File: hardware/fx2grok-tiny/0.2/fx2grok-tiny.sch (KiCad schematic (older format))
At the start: 27 parts, among them IC1 CY7C68013A-56, P1 CONN_01X05, P2 CONN_01X05, U1 MICRO-USB-B-SMD, U2 MIC5504, Y1 24MHz

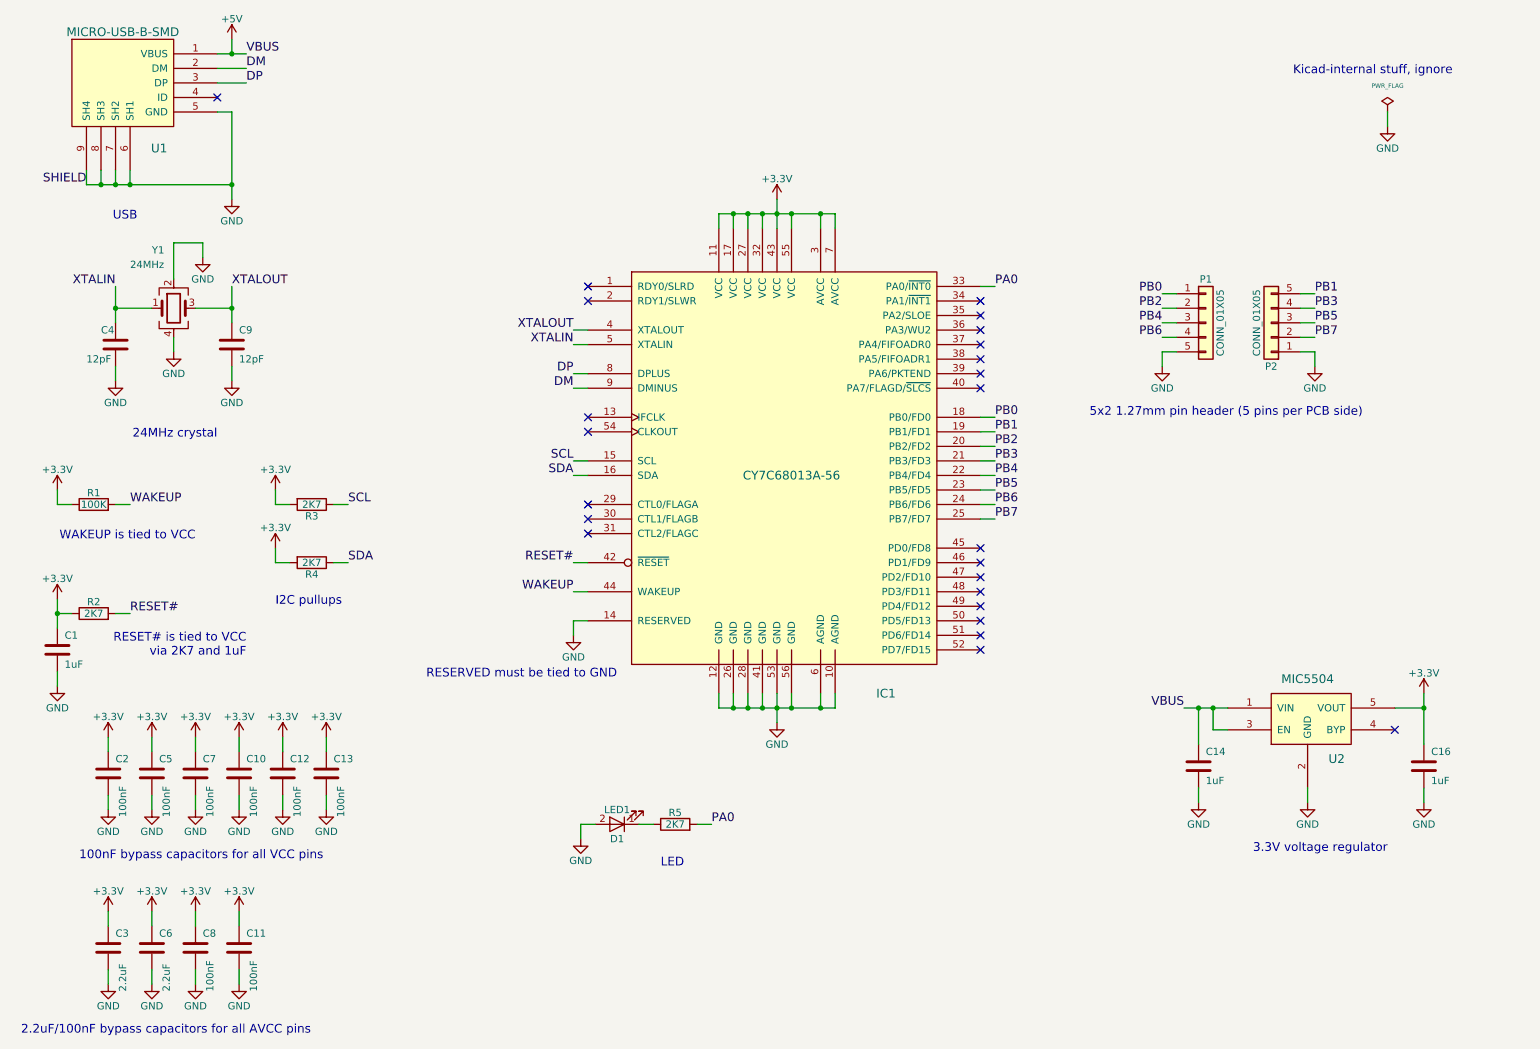
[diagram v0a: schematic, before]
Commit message: fx2grok-tiny: Reroute PCB from scratch with various changes.
 - The previously incorrect FX2 footprint is fixed now.

 - The FX2's thermal pad is set to GND now.

 - The FX2 footprint now has a dot on the copper as well as on the
   silkscreen for pin 1.

 - The PCB is now 11x11mm (instead of 13x13mm).

 - The 1.27mm pin header connectors are shortened and the pinout changed.

 - The trace clearance changed from 6mil to 5mil.

 - The USB connector footprint now has two oval pads (space reasons).

 - The LED is now connected to PA1 (not PA0).

 - The schematics/layout license is changed to CC-BY-SA 4.0.
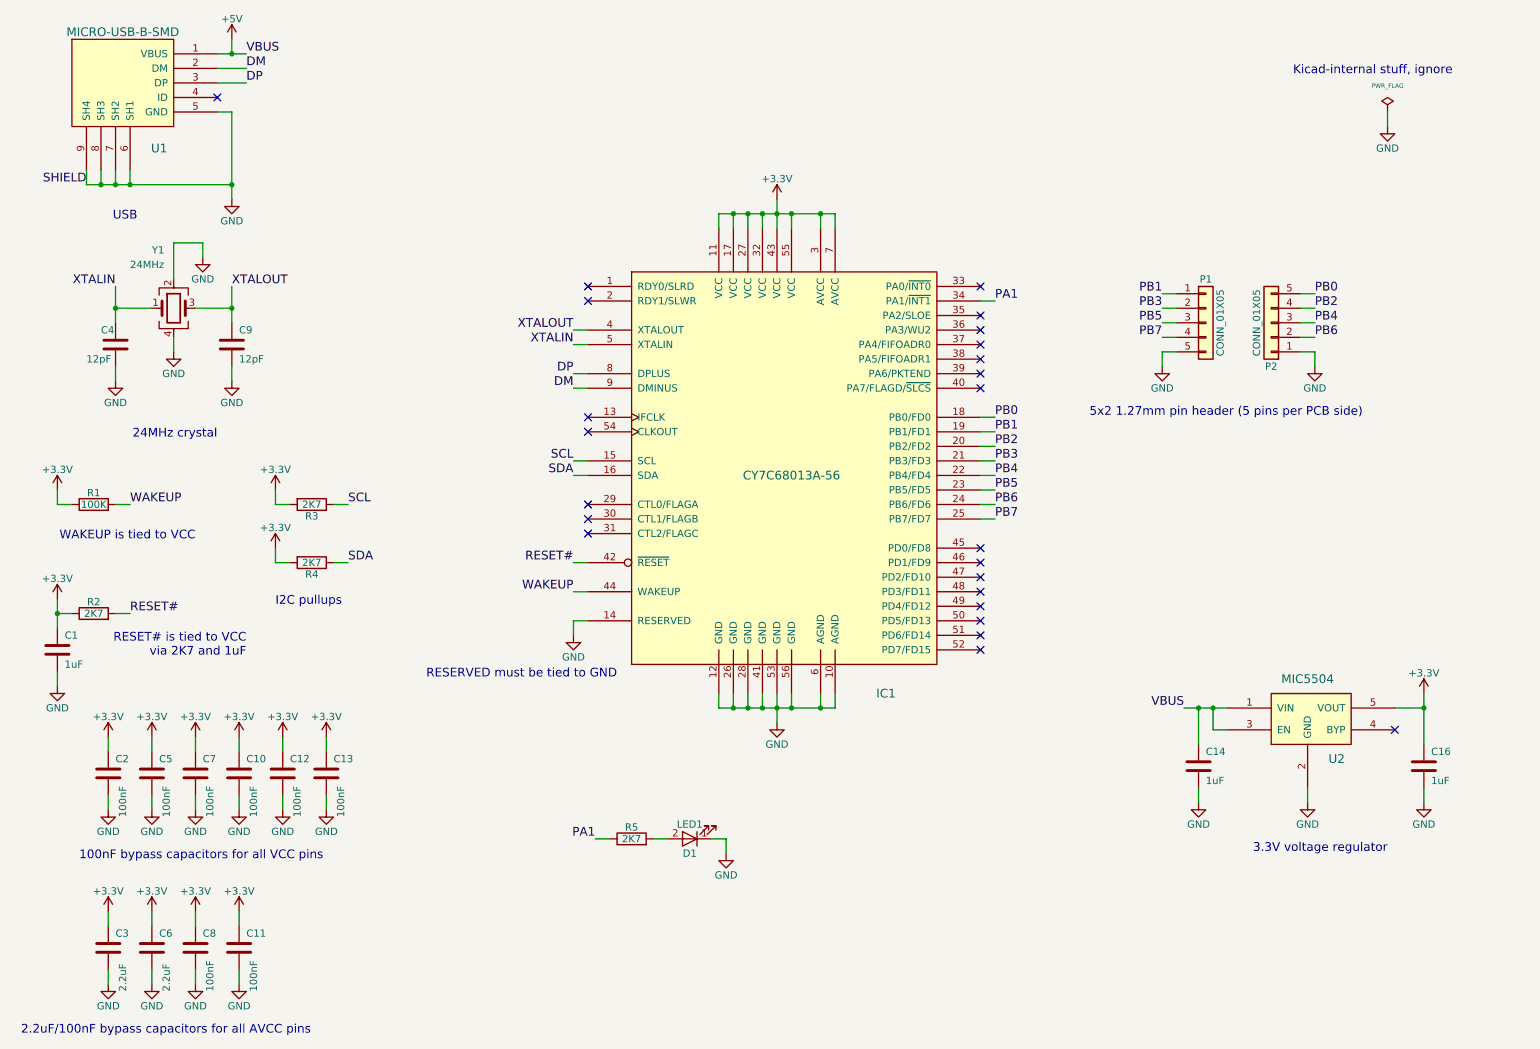
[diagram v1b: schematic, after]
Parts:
- IC1: footprint QFN56 -> fx2grok-tiny:QFN56
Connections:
- net GND: now also D1.1 (K); no longer D1.2 (A)
- net PB0: now also P2.5 (Pin_5); no longer P1.1 (Pin_1)
- net PB1: now also P1.1 (Pin_1); no longer P2.5 (Pin_5)
- net PB2: now also P2.4 (Pin_4); no longer P1.2 (Pin_2)
- net PB3: now also P1.2 (Pin_2); no longer P2.4 (Pin_4)
- net PB4: now also P2.3 (Pin_3); no longer P1.3 (Pin_3)
- net PB5: now also P1.3 (Pin_3); no longer P2.3 (Pin_3)
- net PB6: now also P2.2 (Pin_2); no longer P1.4 (Pin_4)
- net PB7: now also P1.4 (Pin_4); no longer P2.2 (Pin_2)
- net PA1: now reaches IC1.34 (PA1/~INT1)
- net PA1: now also R5.1
- net PA0: no longer names the net of IC1.33 (PA0/~INT0)
- net PA0: no longer R5.2
- new net: D1.2 (A), R5.2
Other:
- note removed: "LED\n"
